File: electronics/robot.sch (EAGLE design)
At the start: 70 parts, among them J1 USB-B, J2 DC21MMX, J3 B6B-ZR, J4 B6B-ZR, J5 B6B-ZR, J6 KICKER, Q1 IRLMS2002TRPBF, Q2 IRLMS2002TRPBF, Q3 NPN_BC817,215, Q4 SUD50N04-8M8P-4GE3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

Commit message: Adding 1uF decoupling for motors
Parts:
- added C18, C21, C22: 1µF, SparkFun-Capacitors:0.33UF/330NF-0805-50V-10%
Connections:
- net GND: now also C18.2, C21.2, C22.2
- net VIN: now also C18.1, C21.1, C22.1
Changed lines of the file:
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@@
 </part>
 <part name="U$1" library="rhoban" deviceset="L102011ML04Q" device=""/>
+<part name="GND2" library="supply1" deviceset="GND" device=""/>
+<part name="GND3" library="supply1" deviceset="GND" device=""/>
+<part name="GND4" library="supply1" deviceset="GND" device=""/>
+<part name="C18" library="SparkFun-Capacitors" deviceset="0.33UF/330NF" device="-0805-50V-10%" value="1µF">
+<attribute name="FARNELL" value="2688486RL"/>
+</part>
+<part name="C21" library="SparkFun-Capacitors" deviceset="0.33UF/330NF" device="-0805-50V-10%" value="1µF">
+<attribute name="FARNELL" value="2688486RL"/>
+<attribute name="PROD_ID" value="CAP-08469"/>
+<attribute name="VALUE" value="0.33µF"/>
+</part>
+<part name="C22" library="SparkFun-Capacitors" deviceset="0.33UF/330NF" device="-0805-50V-10%" value="1µF">
+<attribute name="FARNELL" value="2688486RL"/>
+<attribute name="PROD_ID" value="CAP-08469"/>
+<attribute name="VALUE" value="0.33µF"/>
+</part>
 </parts>
 <sheets>
@@
 <plain>
 <text x="-22.86" y="40.64" size="7.62" layer="97">H BRIDGES</text>
-<frame x1="-38.1" y1="-53.34" x2="63.5" y2="58.42" columns="8" rows="5" layer="95"/>
+<frame x1="-43.18" y1="-76.2" x2="63.5" y2="63.5" columns="8" rows="5" layer="95"/>
 </plain>
 <instances>
@@
 <attribute name="FARNELL" x="17.78" y="-30.48" size="1.778" layer="96" display="off"/>
 </instance>
+<instance part="GND2" gate="1" x="-25.4" y="-60.96"/>
+<instance part="GND3" gate="1" x="-2.54" y="-60.96"/>
+<instance part="GND4" gate="1" x="17.78" y="-60.96"/>
+<instance part="C18" gate="G$1" x="-25.4" y="-53.34">
+<attribute name="FARNELL" x="-25.4" y="-53.34" size="1.778" layer="96" display="off"/>
+</instance>
+<instance part="C21" gate="G$1" x="-2.54" y="-53.34">
+<attribute name="FARNELL" x="-2.54" y="-53.34" size="1.778" layer="96" display="off"/>
+</instance>
+<instance part="C22" gate="G$1" x="17.78" y="-53.34">
+<attribute name="FARNELL" x="17.78" y="-53.34" size="1.778" layer="96" display="off"/>
+</instance>
 </instances>
 <busses>
@@
 <label x="43.18" y="-20.32" size="1.27" layer="95" rot="R180" xref="yes"/>
 </segment>
+<segment>
+<pinref part="GND2" gate="1" pin="GND"/>
+<wire x1="-25.4" y1="-58.42" x2="-25.4" y2="-55.88" width="0.1524" layer="91"/>
+<pinref part="C18" gate="G$1" pin="2"/>
+</segment>
+<segment>
+<pinref part="GND3" gate="1" pin="GND"/>
+<wire x1="-2.54" y1="-58.42" x2="-2.54" y2="-55.88" width="0.1524" layer="91"/>
+<pinref part="C21" gate="G$1" pin="2"/>
+</segment>
+<segment>
+<pinref part="GND4" gate="1" pin="GND"/>
+<wire x1="17.78" y1="-58.42" x2="17.78" y2="-55.88" width="0.1524" layer="91"/>
+<pinref part="C22" gate="G$1" pin="2"/>
+</segment>
 </net>
 <net name="M1A" class="0">
@@
 <pinref part="C3" gate="G$1" pin="1"/>
 </segment>
-</net>
+<segment>
+<wire x1="-25.4" y1="-48.26" x2="-25.4" y2="-43.18" width="0.1524" layer="91"/>
+<label x="-25.4" y="-43.18" size="1.27" layer="95" xref="yes"/>
+<pinref part="C18" gate="G$1" pin="1"/>
+</segment>
+<segment>
+<wire x1="-2.54" y1="-48.26" x2="-2.54" y2="-43.18" width="0.1524" layer="91"/>
+<label x="-2.54" y="-43.18" size="1.27" layer="95" xref="yes"/>
+<pinref part="C21" gate="G$1" pin="1"/>
+</segment>
+<segment>
+<wire x1="17.78" y1="-48.26" x2="17.78" y2="-43.18" width="0.1524" layer="91"/>
+<label x="17.78" y="-43.18" size="1.27" layer="95" xref="yes"/>
+<pinref part="C22" gate="G$1" pin="1"/>
+</segment>
+</net>

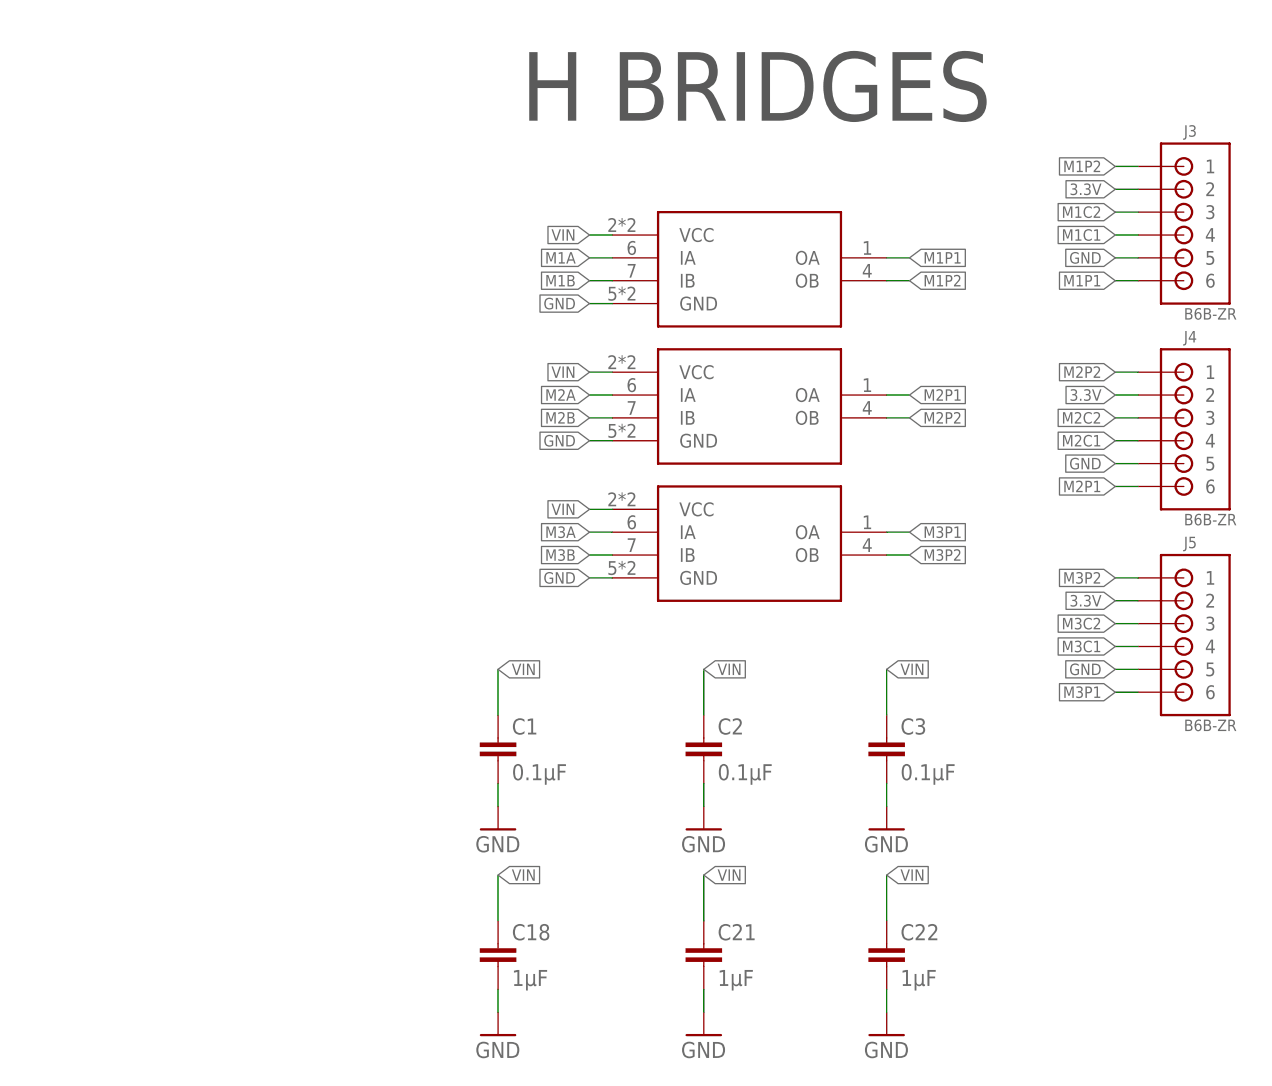
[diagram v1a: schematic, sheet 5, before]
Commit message: Re-routed electronics (not tested)
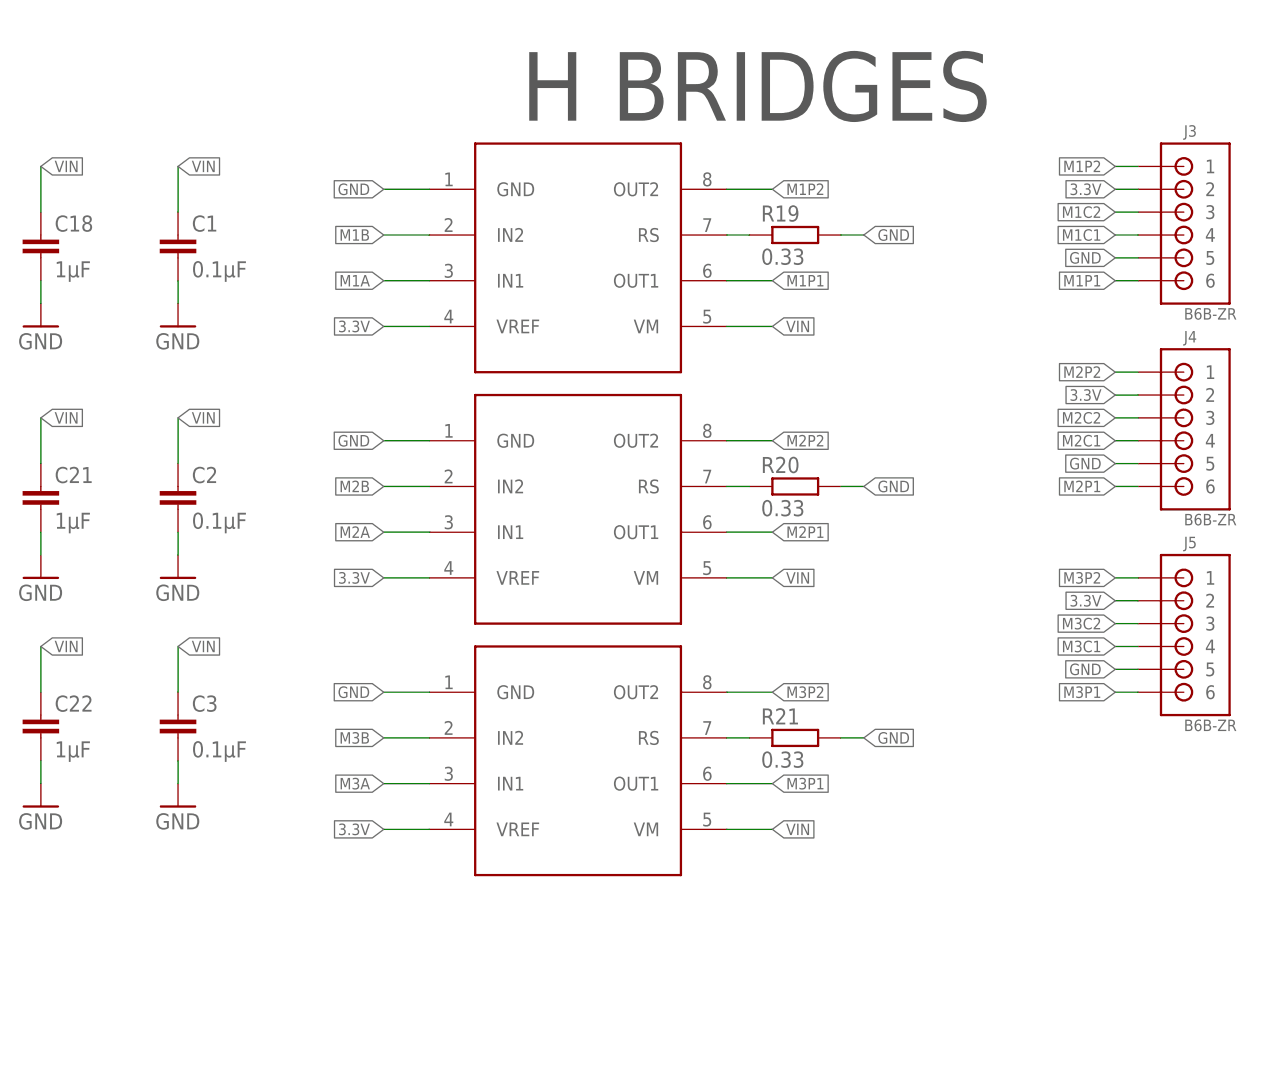
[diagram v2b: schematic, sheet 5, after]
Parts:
- removed U4, U5, U6: L9110, rhoban:L9110
- added R19, R20, R21: 0.33, rcl:R-EU_R1206
- added U$12, U$13, U$7: TB67H450FNG, rhoban:TB67H450FNG
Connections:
- new net N$18: R19.1, U$7.RS
- new net N$20: R20.1, U$12.RS
- new net N$21: R21.1, U$13.RS
- net 3.3V: now also U$12.VREF, U$13.VREF, U$7.VREF
- net GND: now also R19.2, R20.2, R21.2, U$12.GND, U$13.GND, U$7.GND; no longer U4.GND, U5.GND, U6.GND
- net M1A: now also U$7.IN1; no longer U4.IA
- net M1B: now also U$7.IN2; no longer U4.IB
- net M1C1: now also U2.IO25; no longer U2.IO4
- net M1C2: now also U2.IO26; no longer U2.IO16
- net M1P1: now also U$7.OUT1; no longer U4.OA
- net M1P2: now also U$7.OUT2; no longer U4.OB
- net M2A: now also U$12.IN1; no longer U5.IA
- net M2B: now also U$12.IN2; no longer U5.IB
- net M2P1: now also U$12.OUT1; no longer U5.OA
- net M2P2: now also U$12.OUT2; no longer U5.OB
- net M3A: now also U$13.IN1; no longer U6.IA
- net M3B: now also U$13.IN2; no longer U6.IB
- net M3C1: now also U2.IO4; no longer U2.IO25
- net M3C2: now also U2.IO16; no longer U2.IO26
- net M3P1: now also U$13.OUT1; no longer U6.OA
- net M3P2: now also U$13.OUT2; no longer U6.OB
- net VIN: now also U$12.VM, U$13.VM, U$7.VM; no longer U4.VCC, U5.VCC, U6.VCC
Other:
- moved on the sheet: C1, C18, C2, C21, C22, C3
